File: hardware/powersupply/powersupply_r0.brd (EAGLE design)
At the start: 160 x 100 mm, 22 parts, among them CN17 22-23-2041

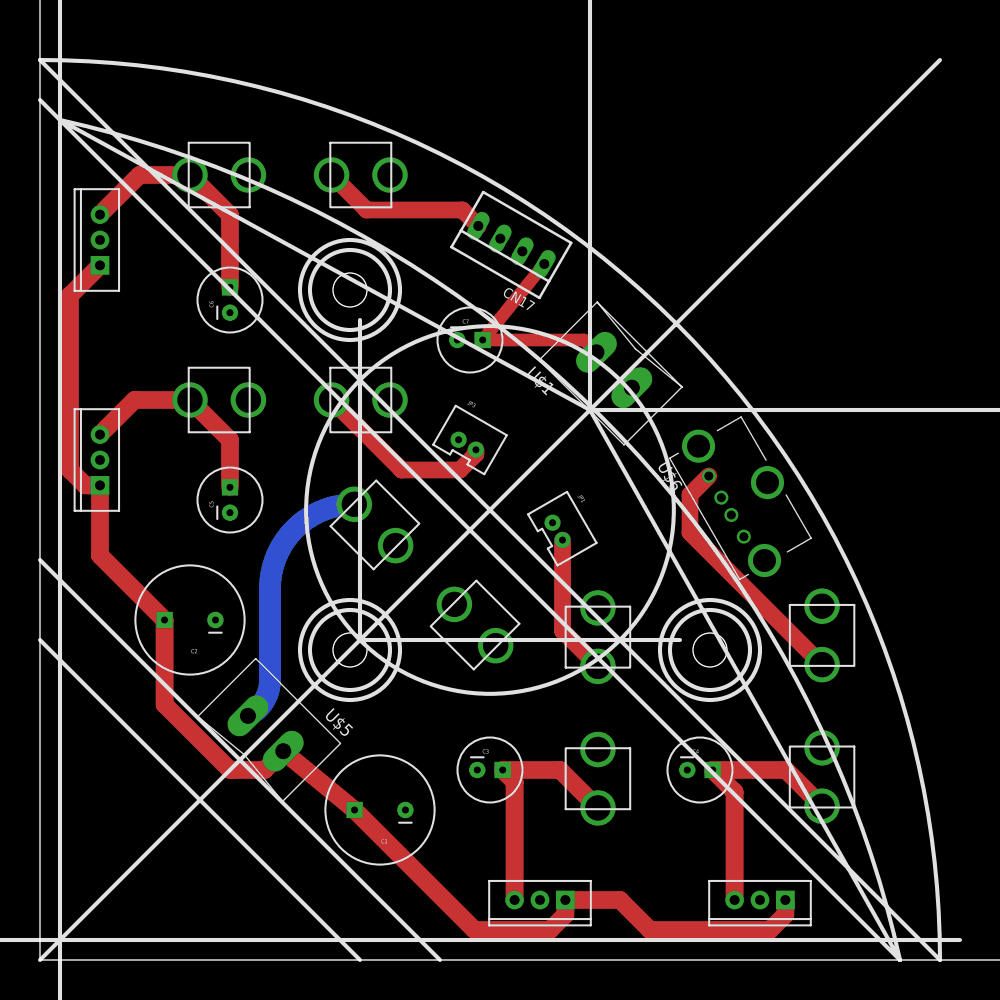
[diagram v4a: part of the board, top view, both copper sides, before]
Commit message: ground plane routing
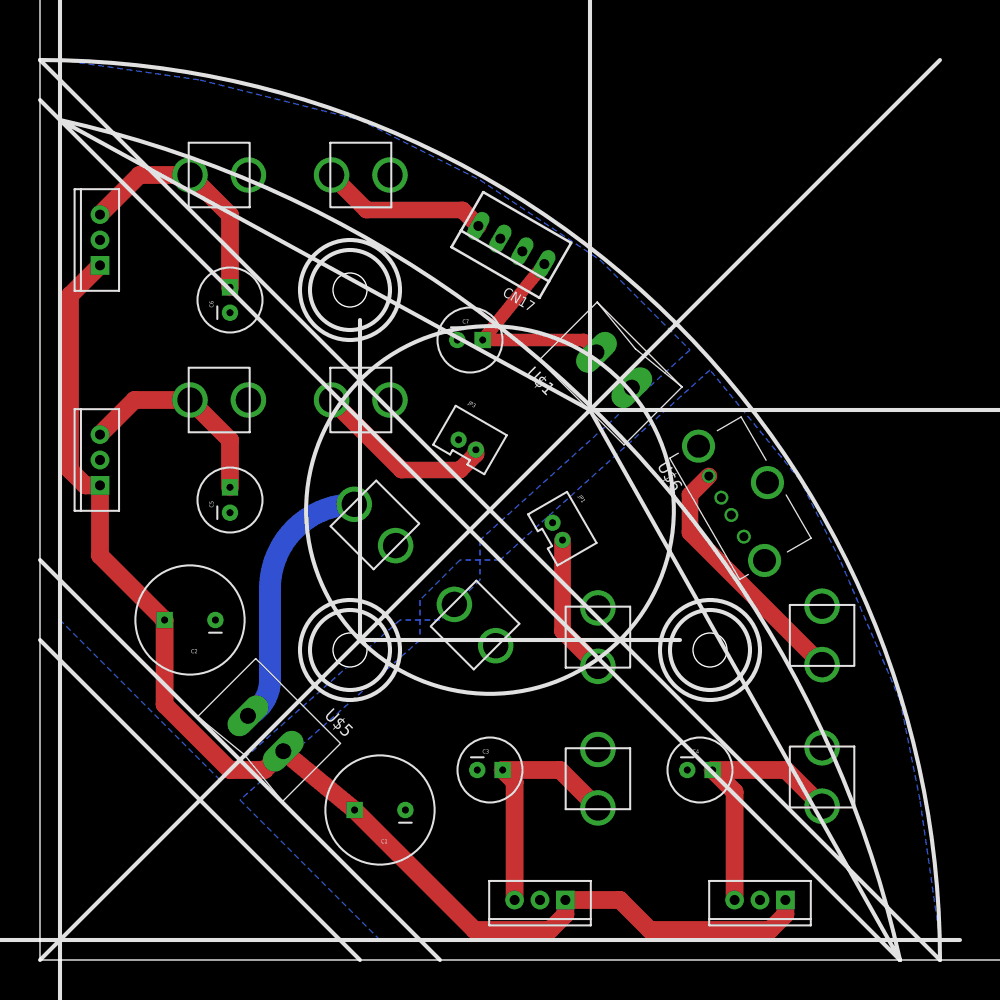
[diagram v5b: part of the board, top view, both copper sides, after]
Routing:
- added copper zone on layer 16, net GND
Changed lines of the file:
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@@
 <setting verticaltext="up"/>
 </settings>
-<grid distance="39.3700787" unitdist="mil" unit="mil" style="lines" multiple="1" display="yes" altdistance="0.025" altunitdist="inch" altunit="inch"/>
+<grid distance="1" unitdist="mm" unit="mm" style="lines" multiple="1" display="yes" altdistance="0.025" altunitdist="inch" altunit="inch"/>
 <layers>
 <layer number="1" name="Top" color="4" fill="1" visible="yes" active="yes"/>
@@
 </class>
 </classes>
-<designrules name="default">
+<designrules name="default *">
 <description language="de">&lt;b&gt;EAGLE Design Rules&lt;/b&gt;
 &lt;p&gt;
@@
 <param name="srMinRoundness" value="0mil"/>
 <param name="srMaxRoundness" value="0mil"/>
-<param name="slThermalIsolate" value="10mil"/>
+<param name="slThermalIsolate" value="12mil"/>
 <param name="slThermalsForVias" value="0"/>
 <param name="dpMaxLengthDifference" value="10mm"/>
@@
 <contactref element="C2" pad="2"/>
 <contactref element="F5" pad="3"/>
-<wire x1="48.233821875" y1="70.865" x2="46.03411875" y2="72.135" width="0" layer="19" extent="1-1"/>
-<wire x1="41.73" y1="62" x2="48.233821875" y2="70.865" width="0" layer="19" extent="1-1"/>
-<wire x1="41.858971875" y1="52.023684375" x2="41.73" y2="62" width="0" layer="19" extent="1-1"/>
-<wire x1="51.255734375" y1="43.725" x2="41.858971875" y2="52.023684375" width="0" layer="19" extent="1-1"/>
-<wire x1="41.440146875" y1="35.55985" x2="51.255734375" y2="43.725" width="0" layer="19" extent="1-1"/>
-<wire x1="59.181978125" y1="57.23223125" x2="51.255734375" y2="43.725" width="0" layer="19" extent="1-1"/>
-<wire x1="43.73" y1="19" x2="41.440146875" y2="35.55985" width="0" layer="19" extent="1-1"/>
-<wire x1="36.54" y1="15" x2="43.73" y2="19" width="0" layer="19" extent="1-1"/>
-<wire x1="50" y1="6" x2="43.73" y2="19" width="0" layer="19" extent="1-1"/>
-<wire x1="70.383971875" y1="42.3349375" x2="59.181978125" y2="57.23223125" width="0" layer="19" extent="1-1"/>
-<wire x1="64.73" y1="19" x2="50" y2="6" width="0" layer="19" extent="1-1"/>
-<wire x1="72" y1="6" x2="64.73" y2="19" width="0" layer="19" extent="1-1"/>
-<wire x1="19" y1="64.73" x2="41.73" y2="62" width="0" layer="19" extent="1-1"/>
-<wire x1="6" y1="72" x2="19" y2="64.73" width="0" layer="19" extent="1-1"/>
-<wire x1="6" y1="50" x2="19" y2="64.73" width="0" layer="19" extent="1-1"/>
-<wire x1="19" y1="44.73" x2="6" y2="50" width="0" layer="19" extent="1-1"/>
-<wire x1="17.54" y1="34" x2="19" y2="44.73" width="0" layer="19" extent="1-1"/>
+<polygon width="0.254" layer="16" spacing="1.778" isolate="0.6096">
+<vertex x="2" y="90"/>
+<vertex x="16" y="88"/>
+<vertex x="32" y="84"/>
+<vertex x="44" y="78"/>
+<vertex x="56" y="70"/>
+<vertex x="65" y="61"/>
+<vertex x="44" y="42"/>
+<vertex x="44" y="38"/>
+<vertex x="40" y="34"/>
+<vertex x="36" y="34"/>
+<vertex x="18" y="18"/>
+<vertex x="2" y="34"/>
+</polygon>
+<polygon width="0.254" layer="16" spacing="1.778" isolate="0.6096">
+<vertex x="90" y="2"/>
+<vertex x="88" y="16"/>
+<vertex x="86" y="26"/>
+<vertex x="80" y="40"/>
+<vertex x="76" y="48"/>
+<vertex x="67" y="59"/>
+<vertex x="46" y="40"/>
+<vertex x="42" y="40"/>
+<vertex x="38" y="36"/>
+<vertex x="38" y="32"/>
+<vertex x="20" y="16"/>
+<vertex x="34" y="2"/>
+</polygon>
 </signal>
 <signal name="N$1">

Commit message: cleanup and silkscreen
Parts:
- renumbered CN17 to CN4, JP1 to CN1, JP3 to CN3, U$1 to CN5, U$5 to CN6, U$6 to CN2
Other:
- board size 160 x 100 mm -> 88 x 88 mm
- board text added: "12V"
- board text added: "40V"
- board text added: "5V"
- board text added: "F1"
- board text added: "F2"
- board text added: "F3"
- board text added: "F4"
- board text added: "F5"
- board text added: "GND"
- board text added: "openct2 power supply (rev0)"
- board text added: "peter jansen / january 2016"
